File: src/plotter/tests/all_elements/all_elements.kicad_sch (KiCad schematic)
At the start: 0 parts

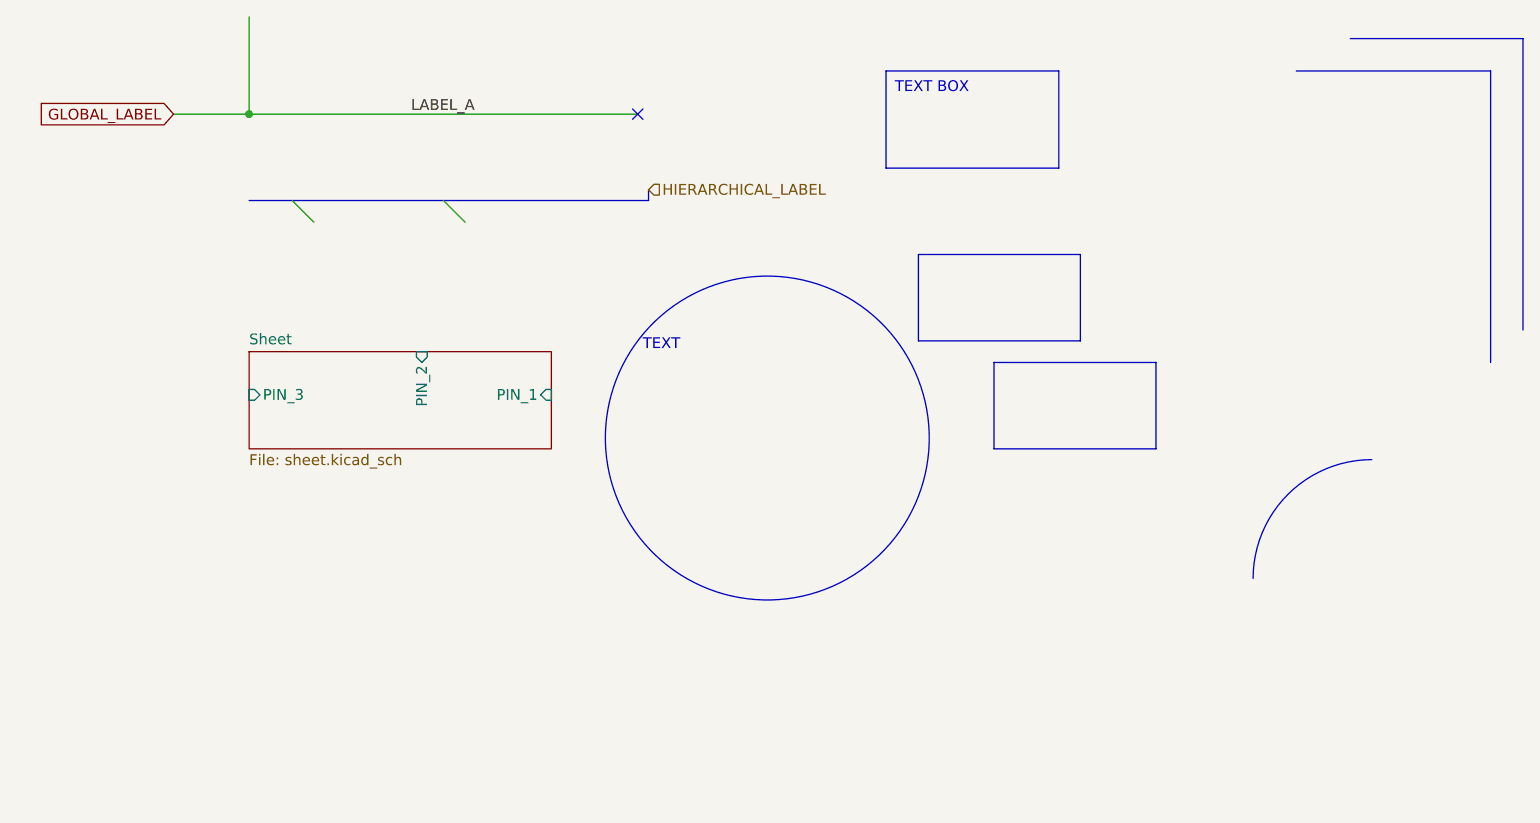
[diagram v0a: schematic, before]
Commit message: update draw arc in plotter and work on docs
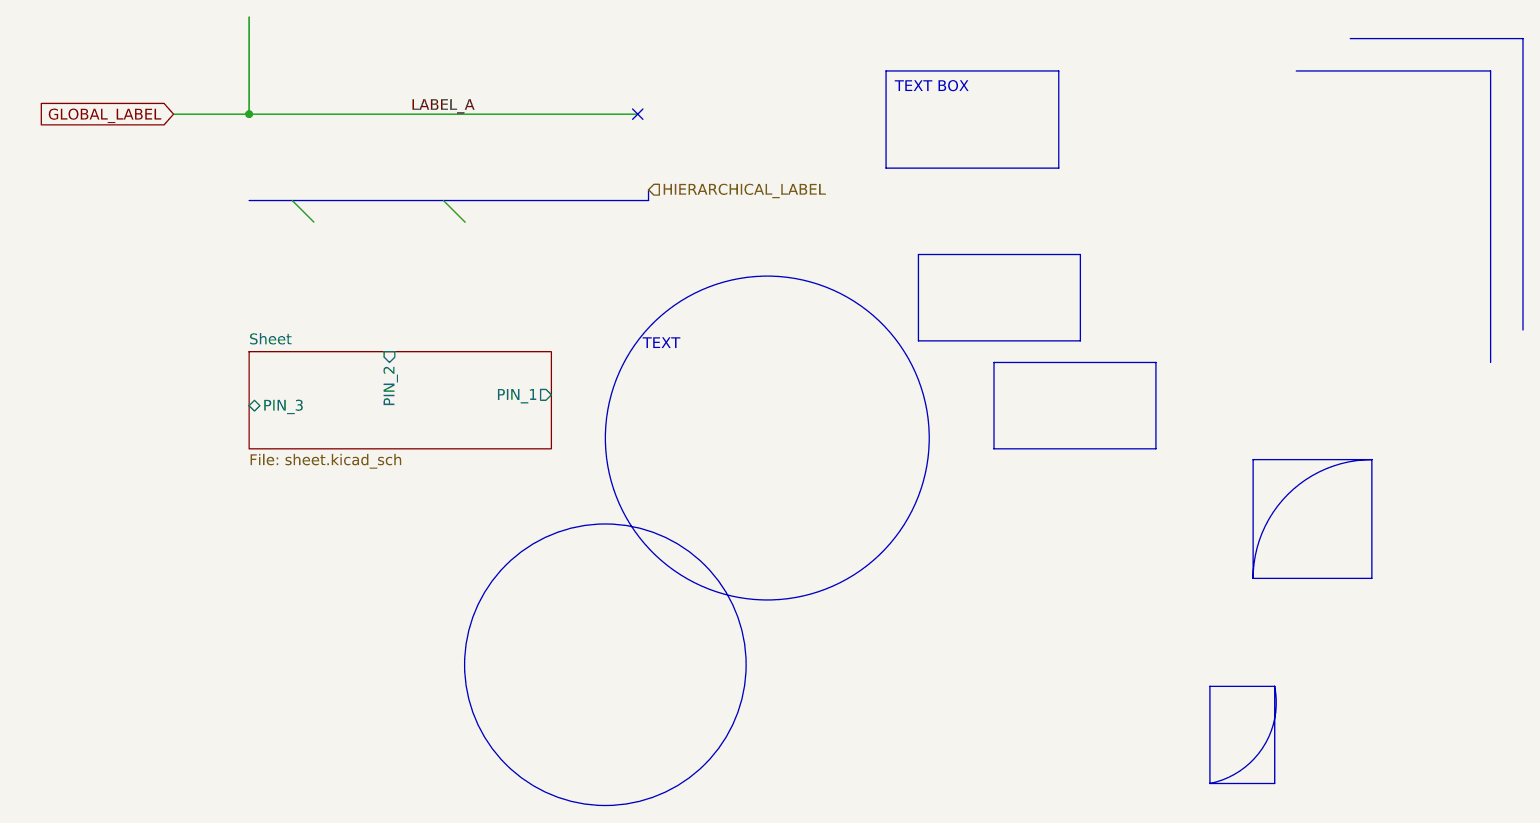
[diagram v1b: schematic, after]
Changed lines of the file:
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@@
+		)
+	)
+	(circle
+		(center 101.6 109.22)
+		(radius 16.5588)
+		(stroke
+			(width 0)
+			(type default)
+			(color 149 255 94 1)
+		)
+		(fill
+			(type color)
+			(color 255 232 28 1)
+		)
+	)
+	(rectangle
+		(start 172.72 111.76)
+		(end 180.34 123.19)
+		(stroke
+			(width 0)
+			(type default)
+		)
+		(fill
+			(type none)
+		)
+	)
+	(rectangle
+		(start 177.8 85.09)
+		(end 191.77 99.06)
+		(stroke
+			(width 0)
+			(type default)
+		)
+		(fill
+			(type none)
 		)
 	)
@@
 		)
 	)
+	(arc
+		(start 180.34 111.76)
+		(mid 178.8972 119.0532)
+		(end 172.72 123.19)
+		(stroke
+			(width 0)
+			(type default)
+		)
+		(fill
+			(type none)
+		)
+	)
 	(rectangle
 		(start 138.43 60.96)
@@
 			)
 		)
-		(pin "PIN_1" input
+		(pin "PIN_2" input
+			(at 76.2 72.39 90)
+			(effects
+				(font
+					(size 1.27 1.27)
+				)
+				(justify right)
+			)
+		)
+		(pin "PIN_1" output
 			(at 95.25 77.47 0)
 			(effects
@@
 			)
 		)
-		(pin "PIN_2" input
-			(at 80.01 72.39 90)
-			(effects
-				(font
-					(size 1.27 1.27)
-				)
-				(justify right)
-			)
-		)
-		(pin "PIN_3" input
-			(at 59.69 77.47 180)
-			(effects
-				(font
+		(pin "PIN_3" bidirectional
+			(at 59.69 78.74 180)
+			(effects
+				(font
